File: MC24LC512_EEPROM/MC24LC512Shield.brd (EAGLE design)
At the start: 39.3 x 26.4 mm, 9 parts, among them U2 EEPROM-I2CSMD

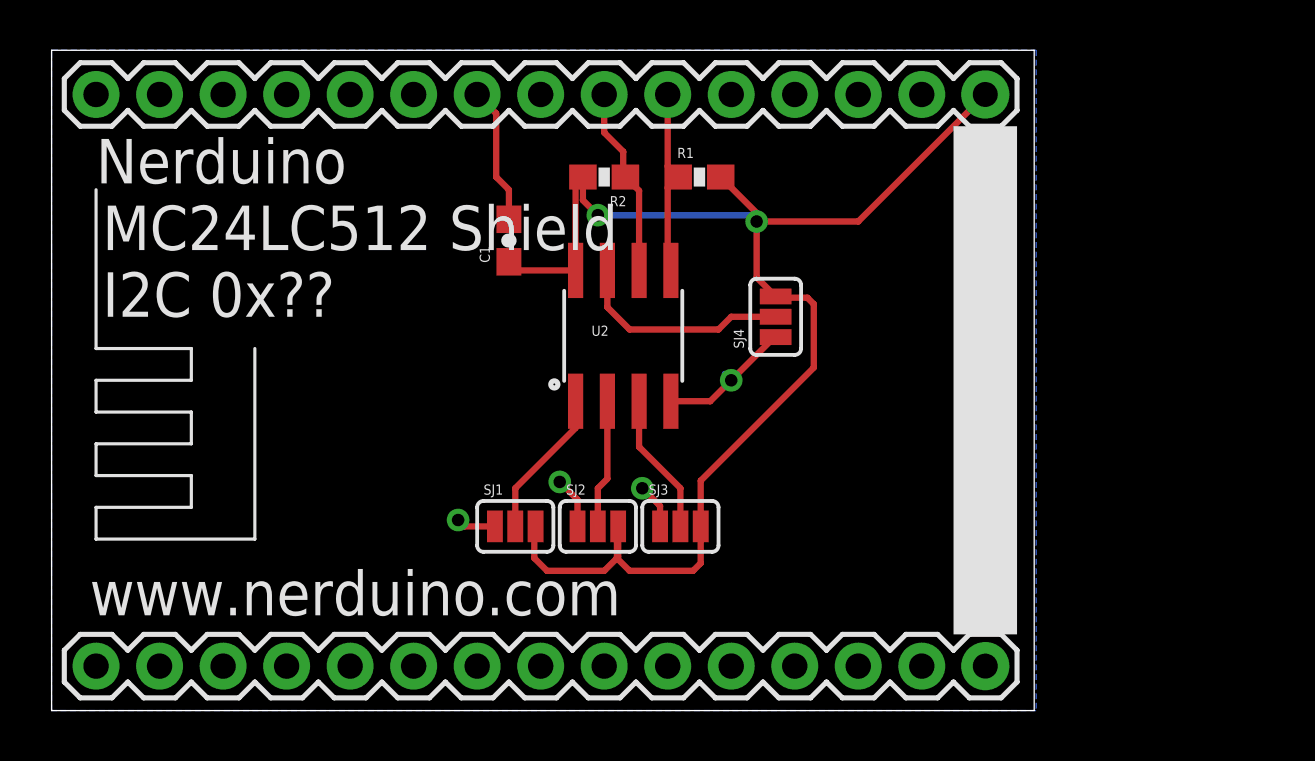
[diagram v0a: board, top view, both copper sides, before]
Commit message: Added OLED Shield Added LiPo Battery Charger Shield Updated outlines of all shields to match the cutout of the nodemcu board
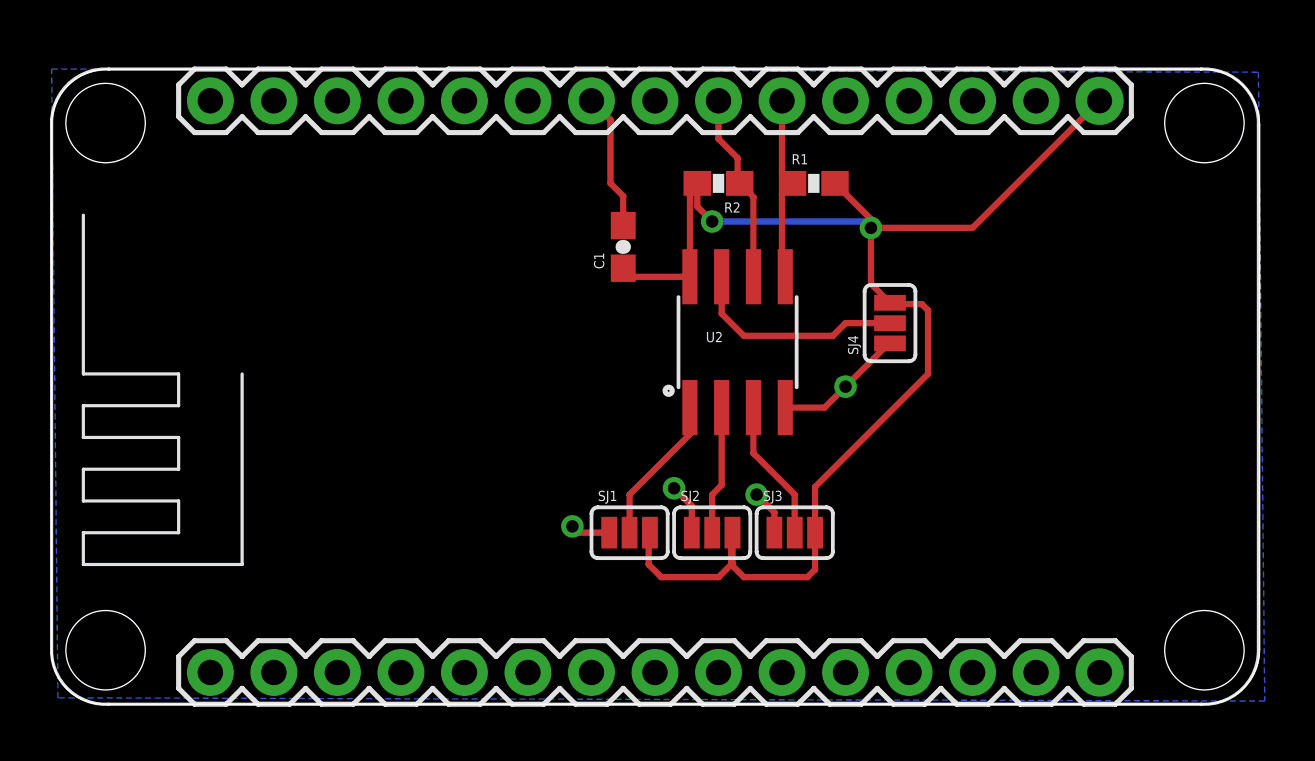
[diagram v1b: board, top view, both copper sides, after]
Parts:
- moved R2 4.58 mm to (26.7, 21.1)
- moved C1 4.58 mm to (22.9, 18.5)
- moved R1 4.58 mm to (30.5, 21.1)
- moved SJ1 4.58 mm to (23.1, 7.11)
- moved SJ2 4.58 mm to (26.4, 7.11)
- moved SJ3 4.58 mm to (29.7, 7.11)
- moved SJ4 4.58 mm to (33.5, 15.5)
- moved U$2 4.58 mm to (24.1, 6.60)
- moved U2 4.58 mm to (27.4, 14.7)
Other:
- board size 39.3 x 26.4 mm -> 48.3 x 25.4 mm
- board text added: "NERDUINO MC24LC512 Shield I2C 0x?? www.nerduino.com"
- board text removed: "MC24LC512 Shield I2C 0x??"
- board text removed: "Nerduino"
- board text removed: "www.nerduino.com"
